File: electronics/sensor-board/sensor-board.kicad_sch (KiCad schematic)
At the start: 32 parts

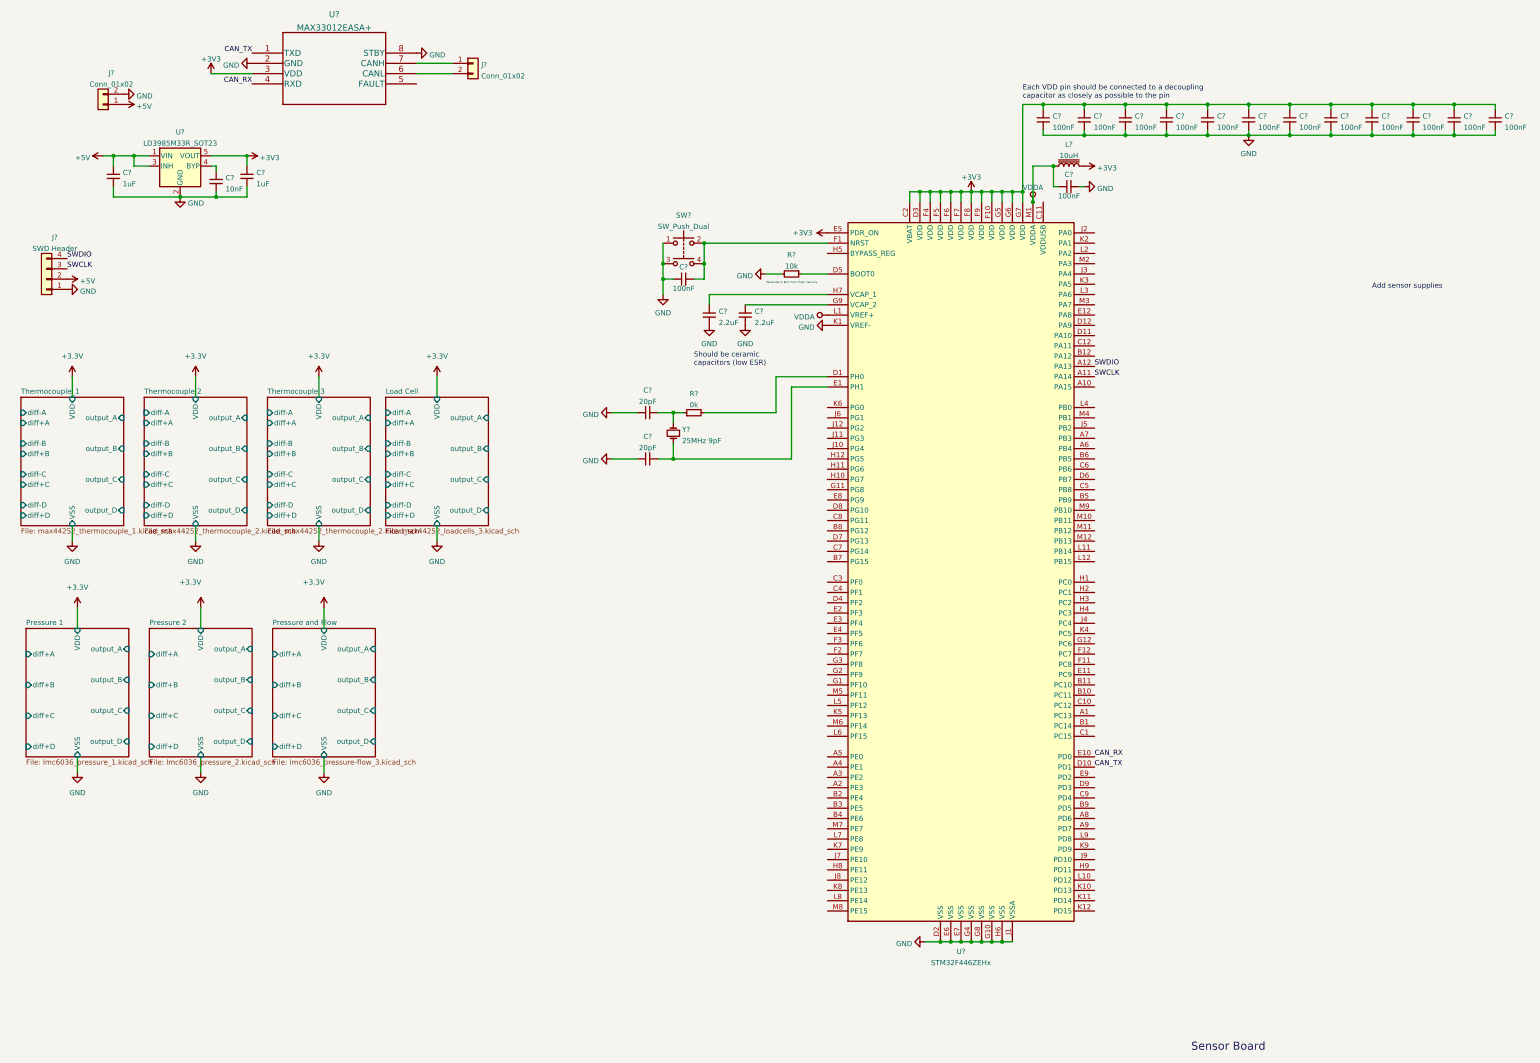
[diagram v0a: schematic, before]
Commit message: work on sensor-board
added MCP960 footprint
finished MCP960 array schematic
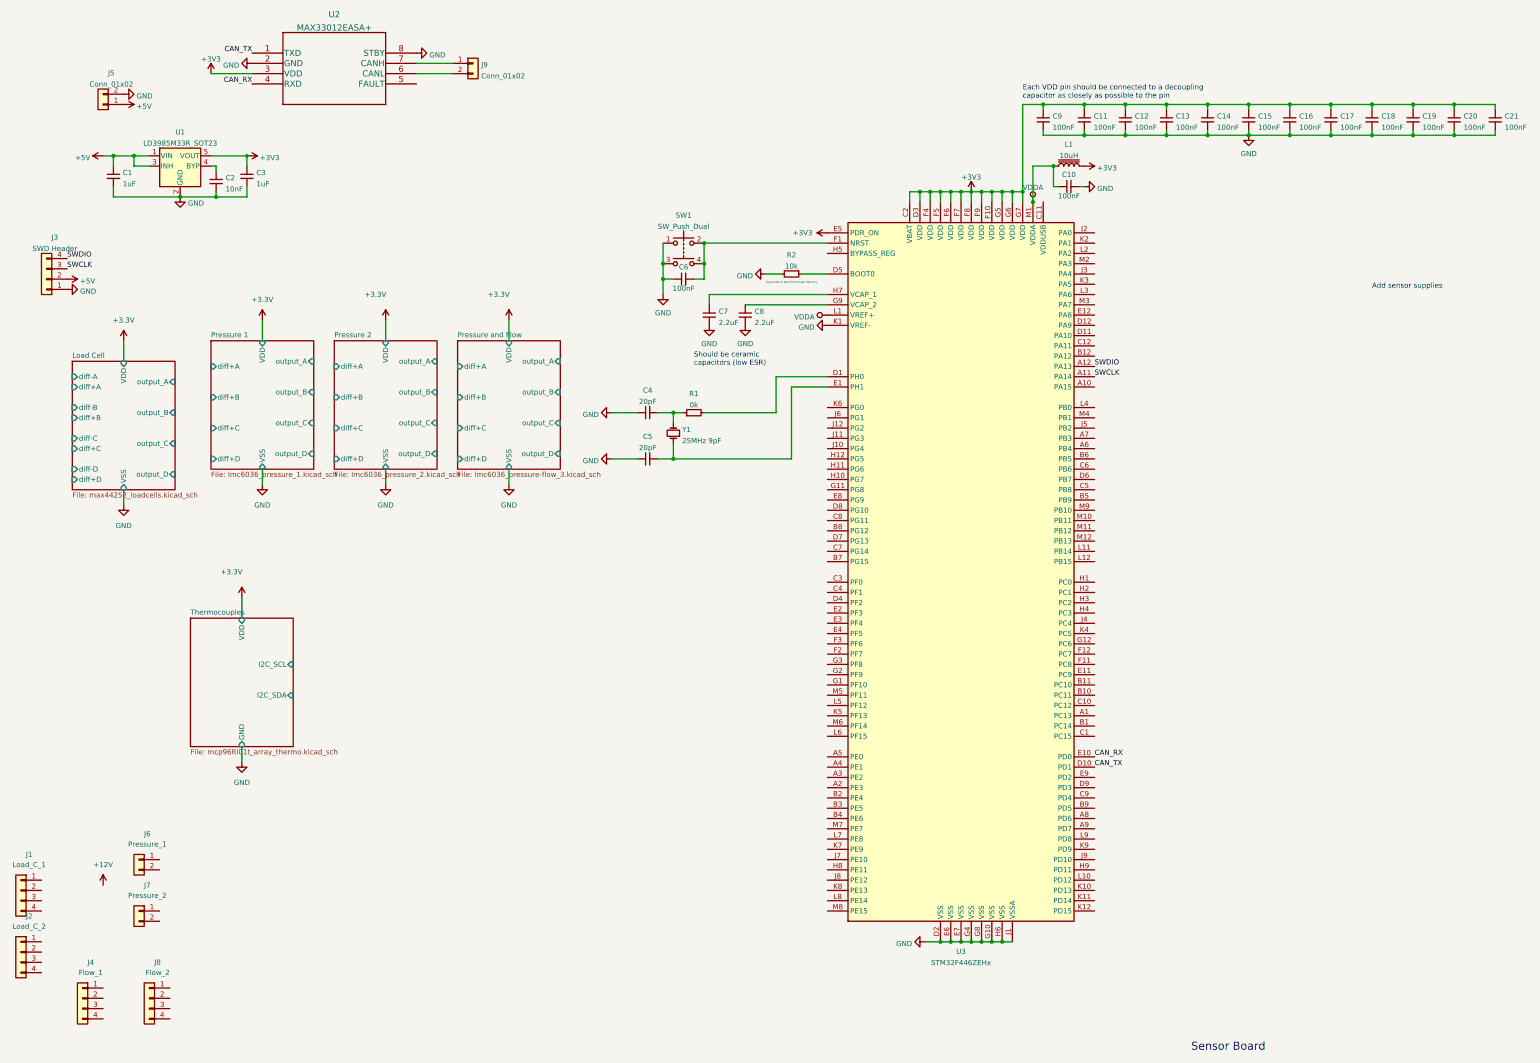
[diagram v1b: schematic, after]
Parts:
- added J1: Load_C_1, symbol Connector_Generic:Conn_01x04
- added J2: Load_C_2, symbol Connector_Generic:Conn_01x04
- added J4: Flow_1, symbol Connector_Generic:Conn_01x04
- added J6: Pressure_1, symbol Connector_Generic:Conn_01x02
- added J7: Pressure_2, symbol Connector_Generic:Conn_01x02
- added J8: Flow_2, symbol Connector_Generic:Conn_01x04
- C1, C10, C11, C12, C13, C14, C15, C16, C17, C18, C19, C2, C20, C21, C3, C4, C5, C6, C7, C8, C9: renamed from C?; footprint (none) -> Capacitor_SMD:C_0603_1608Metric
- R1, R2: renamed from R?; footprint (none) -> Resistor_SMD:R_0603_1608Metric
- U2: renamed from U?; footprint 21-0041-3-M_90-0096-8L_MXM -> MAX33012EASA+:MAX33012EASA+
- gave numbers to parts that had none: 8
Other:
- removed sheet Thermocouple 2
- removed sheet Thermocouple 3
- removed sheet Thermocouple_1
- added sheet Thermocouples (mcp96Rl01t_array_thermo.kicad_sch)
- sheet Load Cell: file max44252_loadcells_3.kicad_sch -> max44252_loadcells.kicad_sch

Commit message: work on sensor-board
thermocouple connector footprints made (selected connector)
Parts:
- added J17: Pressure_7, symbol Connector_Generic:Conn_01x02
- added J18: Pressure_8, symbol Connector_Generic:Conn_01x02
- added J19, J20: Conn_01x02, symbol Connector_Generic:Conn_01x02
- added J21: Pressure_5, symbol Connector_Generic:Conn_01x02
- added J22: Pressure_1, symbol Connector_Generic:Conn_01x02
- added J23: Pressure_2, symbol Connector_Generic:Conn_01x02
- added J24: Pressure_3, symbol Connector_Generic:Conn_01x02
- added J25: Pressure_4, symbol Connector_Generic:Conn_01x02
- J4, J8: footprint (none) -> Connector_PinHeader_2.54mm:PinHeader_1x04_P2.54mm_Horizontal
- J6: value Pressure_1 -> Pressure_5; footprint (none) -> Connector_PinHeader_2.54mm:PinHeader_1x04_P2.54mm_Horizontal
- J7: value Pressure_2 -> Pressure_6; footprint (none) -> Connector_PinHeader_2.54mm:PinHeader_1x04_P2.54mm_Horizontal
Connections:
- net +12V: now also J1.1 (Pin_1), J2.1 (Pin_1), J6.1 (Pin_1), J7.1 (Pin_1), J17.1 (Pin_1), J18.1 (Pin_1), J20.1 (Pin_1), J21.1 (Pin_1), J22.1 (Pin_1), J23.1 (Pin_1), J24.1 (Pin_1), J25.1 (Pin_1)
- net GND: now also J1.4 (Pin_4), J2.4 (Pin_4), J4.4 (Pin_4), J8.4 (Pin_4), J19.2 (Pin_2), J20.2 (Pin_2)
- net Load Cell/diff+A: now also J1.3 (Pin_3)
- net Load Cell/diff+B: now also J2.3 (Pin_3)
- net Load Cell/diff-A: now also J1.2 (Pin_2)
- net Load Cell/diff-B: now also J2.2 (Pin_2)
- net Pressure 1/diff+A: now also J22.2 (Pin_2)
- net Pressure 1/diff+B: now also J23.2 (Pin_2)
- net Pressure 1/diff+C: now also J24.2 (Pin_2)
- net Pressure 1/diff+D: now also J25.2 (Pin_2)
- net Pressure 2/diff+A: now also J6.2 (Pin_2)
- net Pressure 2/diff+B: now also J7.2 (Pin_2)
- net Pressure 2/diff+C: now also J17.2 (Pin_2)
- net Pressure 2/diff+D: now also J18.2 (Pin_2)
- net Pressure and Flow/diff+A: now also J21.2 (Pin_2)
- net Pressure and Flow/diff+B: now also J4.3 (Pin_3)
- net Pressure and Flow/diff+C: now also J8.3 (Pin_3)
- net +24V: now reaches J4.1 (Pin_1)
- net +24V: now also J8.1 (Pin_1), J19.1 (Pin_1)
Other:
- moved on the sheet: C10, C11, C12, C13, C14, C15, C16, C17, C18, C19, C20, C21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

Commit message: work on sensor-board
finishing sub-circuits
switching mcu to stm32f105
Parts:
- removed U3: STM32F446ZEHx, Package_BGA:UFBGA-144_7x7mm_Layout12x12_P0.5mm, symbol MCU_ST_STM32F4:STM32F446ZEHx
- added U? (x3): STM32F105VBH6, LFBGA100, symbol STM32F105VBH6:STM32F105VBH6
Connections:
- net +3V3: now also U?.B2 (VBAT), U?.D2 (VDD_5), U?.F4 (VDD_4), U?.F5 (VDD_3), U?.F6 (VDD_2), U?.F7 (VDD_1)
- net GND: now also U?.C2 (VSS_5), U?.E4 (VSS_4), U?.E5 (VSS_3), U?.E6 (VSS_2), U?.E7 (VSS_1), U?.G1 (VSSA), U?.H1 (VREF-)
- net VDDA: now also U?.J1 (VREF+), U?.K1 (VDDA)
- net at C5.2, Y1.1: now also U?.C1 (OSC_IN)
- net at C6.2, SW1.2, SW1.4: now also U?.E1 (NRST)
- net at R1.2: now also U?.D1 (OSC_OUT)
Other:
- note removed: "Add sensor supplies"
- moved on the sheet: C10, C11, C12, C13, C14, C15, C16, C17, C18, C19, C20, C21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

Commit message: Finalized sensor-board schematic
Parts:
- removed C13, C14, C15, C16, C17, C18, C19, C20, C21: 100nF, Capacitor_SMD:C_0603_1608Metric, symbol Device:C_Small
- removed U? (x3): STM32F105VBH6, LFBGA100, symbol STM32F105VBH6:STM32F105VBH6
- added J19: Spare_1, Connector_PinHeader_2.54mm:PinHeader_1x02_P2.54mm_Horizontal, symbol Connector_Generic:Conn_01x02
- added J20: Spare_2, Connector_PinHeader_2.54mm:PinHeader_1x02_P2.54mm_Horizontal, symbol Connector_Generic:Conn_01x02
- added J21: Spare_3, Connector_PinHeader_2.54mm:PinHeader_1x02_P2.54mm_Horizontal, symbol Connector_Generic:Conn_01x02
- added J22: Spare_4, Connector_PinHeader_2.54mm:PinHeader_1x02_P2.54mm_Horizontal, symbol Connector_Generic:Conn_01x02
- added U3: STM32L051R6Tx, Package_QFP:LQFP-64_10x10mm_P0.5mm, symbol MCU_ST_STM32L0:STM32L051R6Tx
- C7, C8: value 2.2uF -> 100nF
- J10: renamed from J5; value Conn_01x02 -> Suppply_5V; footprint (none) -> Connector_PinHeader_2.54mm:PinHeader_1x02_P2.54mm_Horizontal
- J11: renamed from J22; footprint (none) -> Connector_PinHeader_2.54mm:PinHeader_1x02_P2.54mm_Horizontal
- J12: renamed from J23; footprint (none) -> Connector_PinHeader_2.54mm:PinHeader_1x02_P2.54mm_Horizontal
- J13: renamed from J24; footprint (none) -> Connector_PinHeader_2.54mm:PinHeader_1x02_P2.54mm_Horizontal
- J14: renamed from J25; footprint (none) -> Connector_PinHeader_2.54mm:PinHeader_1x02_P2.54mm_Horizontal
- J15: renamed from J21; footprint (none) -> Connector_PinHeader_2.54mm:PinHeader_1x02_P2.54mm_Horizontal
- J18: renamed from J9; value Conn_01x02 -> CAN_Bus
- J2: renamed from J19; value Conn_01x02 -> Supply_24V; footprint (none) -> Connector_PinHeader_2.54mm:PinHeader_1x02_P2.54mm_Horizontal
- J3: renamed from J20; value Conn_01x02 -> Supply_12V; footprint (none) -> Connector_PinHeader_2.54mm:PinHeader_1x02_P2.54mm_Horizontal
- J4: renamed from J1; footprint (none) -> Connector_PinHeader_2.54mm:PinHeader_1x04_P2.54mm_Horizontal
- J5: renamed from J2; footprint (none) -> Connector_PinHeader_2.54mm:PinHeader_1x04_P2.54mm_Horizontal
- J8: renamed from J17; footprint (none) -> Connector_PinHeader_2.54mm:PinHeader_1x02_P2.54mm_Horizontal
- J9: renamed from J18; footprint (none) -> Connector_PinHeader_2.54mm:PinHeader_1x02_P2.54mm_Horizontal
- L1: footprint (none) -> Inductor_SMD:L_0603_1608Metric
- SW1: footprint (none) -> Custom_button_CS1102:Button CS1102
- renumbered J3 to J1, J4 to J16, J8 to J17
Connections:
- net +12V: now also J19.1 (Pin_1), J20.1 (Pin_1), J21.1 (Pin_1), J22.1 (Pin_1)
- net +3V3: now also C7.1, C8.1, U3.1 (VLCD), U3.19 (VDD), U3.32 (VDD), U3.48 (VDDIO2), U3.64 (VDD)
- net GND: now also U3.12 (VSSA), U3.18 (VSS), U3.31 (VSS), U3.47 (VSS), U3.63 (VSS)
- net SWCLK: now also U3.49 (PA14)
- net SWDIO: now also U3.46 (PA13)
- net VDDA: now also U3.13 (VDDA)
- net at C5.2, Y1.1: now also U3.6 (PH1)
- net at C6.2, SW1.2, SW1.4: now also U3.7 (NRST)
- net at R1.2: now also U3.5 (PH0)
- net at R2.1: now also U3.60 (BOOT0)
- new net ADC12_IN0: U3.14 (PA0)
- new net ADC12_IN1: U3.15 (PA1)
- new net ADC12_IN10: U3.8 (PC0)
- new net ADC12_IN11: U3.9 (PC1)
- new net ADC12_IN12: U3.10 (PC2)
- new net ADC12_IN13: U3.11 (PC3)
- new net ADC12_IN14: U3.24 (PC4)
- new net ADC12_IN15: U3.25 (PC5)
- new net ADC12_IN2: U3.16 (PA2)
- new net ADC12_IN3: U3.17 (PA3)
- new net ADC12_IN4: U3.20 (PA4)
- new net ADC12_IN5: U3.21 (PA5)
- new net ADC12_IN6: U3.22 (PA6)
- new net ADC12_IN7: U3.23 (PA7)
- new net ADC12_IN8: U3.26 (PB0)
- new net ADC12_IN9: U3.27 (PB1)
- new net I2C1_SCL: U3.58 (PB6)
- new net I2C1_SDA: U3.59 (PB7)
- new net I2C2_SCL: U3.29 (PB10)
- new net I2C2_SDA: U3.30 (PB11)
- new net SPARE_gen_purp_amp/diff+A: J19.2 (Pin_2)
- new net SPARE_gen_purp_amp/diff+B: J20.2 (Pin_2)
- new net SPARE_gen_purp_amp/diff+C: J21.2 (Pin_2)
- new net SPARE_gen_purp_amp/diff+D: J22.2 (Pin_2)
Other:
- added sheet SPARE_gen_purp_amp (lmc6036_pressure_SPARE.kicad_sch)
- note removed: "Should be ceramic capacitors (low ESR)"
- moved on the sheet: J1, J10, J11, J12, J13, J14, J15, J16, J17, J2, J3, J4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

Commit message: work on sensor-board
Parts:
- removed C4, C5: 20pF, Capacitor_SMD:C_0603_1608Metric, symbol Device:C_Small
- removed R1: 0k, Resistor_SMD:R_0603_1608Metric, symbol Device:R_Small
- removed R2: 10k, Resistor_SMD:R_0603_1608Metric, symbol Device:R_Small
- removed U3: STM32L051R6Tx, Package_QFP:LQFP-64_10x10mm_P0.5mm, symbol MCU_ST_STM32L0:STM32L051R6Tx
- added C27: 20pF, Capacitor_SMD:C_0603_1608Metric, symbol Device:C_Small
- added C28, C29: 100nF, Capacitor_SMD:C_0603_1608Metric, symbol Device:C_Small
- added J30: Spare_HR, Connector_PinHeader_2.54mm:PinHeader_1x04_P2.54mm_Horizontal, symbol Connector_Generic:Conn_01x04
- added R108, R2: TO CALCULATE 4.7k, Resistor_SMD:R_0603_1608Metric, symbol Device:R
- added R109, R110: 100, Resistor_SMD:R_0603_1608Metric, symbol Device:R
- added R111: 10k, Resistor_SMD:R_0603_1608Metric, symbol Device:R_Small
- added R112: 0k, Resistor_SMD:R_0603_1608Metric, symbol Device:R_Small
- added U3: STM32F105VBH6, STM32F105VBH6:STM32F105VBH6, symbol STM32F105VBH6:STM32F105VBH6
- C12: value 100nF -> 20pF
- J15: value Pressure_5 -> Pressure_9
- J18, Y1: footprint (none) -> Resistor_THT:R_Axial_DIN0204_L3.6mm_D1.6mm_P1.90mm_Vertical
- J6, J7: footprint Connector_PinHeader_2.54mm:PinHeader_1x04_P2.54mm_Horizontal -> Connector_PinHeader_2.54mm:PinHeader_1x02_P2.54mm_Horizontal
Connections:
- net +12V: now also J30.1 (Pin_1)
- net +3V3: now also C10.1, C6.1, C29.1, U3.B2 (VBAT), U3.D2 (VDD_5), U3.F4 (VDD_4), U3.F5 (VDD_3), U3.F6 (VDD_2), U3.F7 (VDD_1); no longer C12.1, C8.1
- net ADC12_IN0: now also U3.G2 (PA0-WKUP)
- net ADC12_IN1: now also U3.H2 (PA1)
- net ADC12_IN10: now also U3.F1 (PC0)
- net ADC12_IN11: now also U3.F2 (PC1)
- net ADC12_IN12: now also U3.E2 (PC2)
- net ADC12_IN13: now also U3.F3 (PC3)
- net ADC12_IN14: now also U3.G4 (PC4)
- net ADC12_IN15: now also U3.H4 (PC5)
- net ADC12_IN2: now also U3.J2 (PA2)
- net ADC12_IN3: now also U3.K2 (PA3)
- net ADC12_IN4: now also U3.G3 (PA4)
- net ADC12_IN5: now also U3.H3 (PA5)
- net ADC12_IN6: now also U3.J3 (PA6)
- net ADC12_IN7: now also U3.K3 (PA7)
- net ADC12_IN8: now also U3.J4 (PB0)
- net ADC12_IN9: now also U3.K4 (PB1)
- net CAN_RX: now also U3.C10 (PA11)
- net CAN_TX: now also U3.B10 (PA12)
- net GND: now also C12.1, C6.2, C27.1, C28.1, C29.2, J30.4 (Pin_4), R111.2, U3.C2 (VSS_5), U3.E4 (VSS_4), U3.E5 (VSS_3), U3.E6 (VSS_2), U3.E7 (VSS_1), U3.G1 (VSSA), U3.H1 (VREF-); no longer C12.2, C6.1
- net I2C1_SCL: now also R109.1, R2.2
- net I2C1_SDA: now also R108.2, R110.1
- net I2C2_SCL: now also U3.J7 (PB10)
- net I2C2_SDA: now also U3.K7 (PB11)
- net Load Cell/diff+C: now also J30.3 (Pin_3)
- net Load Cell/diff-C: now also J30.2 (Pin_2)
- net SWCLK: now also U3.A9 (PA14)
- net SWDIO: now also U3.A10 (PA13)
- net VDDA: now also C8.1, U3.J1 (VREF+), U3.K1 (VDDA); no longer C10.1
- net at Y1.1: now also C12.2, U3.C1 (OSC_IN)
- net at Y1.2: now also C27.2, R112.1
- net at SW1.2, SW1.4: now also C28.2, U3.E1 (NRST); no longer C6.2
- new net: R112.2, U3.D1 (OSC_OUT)
- new net: R110.2, U3.A5 (PB7)
- new net: R109.2, U3.B5 (PB6)
- new net: R111.1, U3.D5 (BOOT0)
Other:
- note added: "NOT USED"
- note removed: "Hardcode to boot from flash memory"
- moved on the sheet: J1, J10, J4, J5

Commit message: work on sensor-board pcb
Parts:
- removed Y1: 25MHz 9pF, Resistor_THT:R_Axial_DIN0204_L3.6mm_D1.6mm_P1.90mm_Vertical, symbol Device:Crystal_Small
- added Y1: Crystal_GND24, Crystal:Crystal_SMD_3225-4Pin_3.2x2.5mm, symbol Device:Crystal_GND24
- J18: footprint Resistor_THT:R_Axial_DIN0204_L3.6mm_D1.6mm_P1.90mm_Vertical -> Connector_PinHeader_2.54mm:PinHeader_1x02_P2.54mm_Horizontal
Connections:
- net GND: now also Y1.1, Y1.3
- net at C27.2, R112.1: now also Y1.4
- net at C12.2, U3.C1 (OSC_IN): now also Y1.2
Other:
- moved on the sheet: C27, R112

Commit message: work on sensor-board pcb
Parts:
- added J31: Spare_HR_2, Custom_Molex_SL_2.54:SL_2.54_H_4pin, symbol Connector_Generic:Conn_01x04
- added TP1, TP2, TP3, TP4, TP5, TP6, TP7: TestPoint, TestPoint:TestPoint_Pad_D2.0mm, symbol Connector:TestPoint
- J10, J11, J12, J13, J14, J15, J18, J19, J2, J20, J21, J22, J3, J6, J7, J8, J9: footprint Connector_PinHeader_2.54mm:PinHeader_1x02_P2.54mm_Horizontal -> Custom_Molex_SL_2.54:SL_2.54_H_2pin
- J16, J17, J4, J5: footprint Connector_PinHeader_2.54mm:PinHeader_1x04_P2.54mm_Horizontal -> Custom_Molex_SL_2.54:SL_2.54_H_4pin
- J30: value Spare_HR -> Spare_HR_1; footprint Connector_PinHeader_2.54mm:PinHeader_1x04_P2.54mm_Horizontal -> Custom_Molex_SL_2.54:SL_2.54_H_4pin
- R108, R2: value TO CALCULATE 4.7k -> 4.7k
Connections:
- net +12V: now also J31.1 (Pin_1); no longer J19.1 (Pin_1), J20.1 (Pin_1), J21.1 (Pin_1), J22.1 (Pin_1)
- net +3V3: now also R108.1, R2.1
- net ADC12_IN13: now also TP5.1
- net ADC12_IN14: now also TP6.1
- net ADC12_IN15: now also TP7.1
- net GND: now also J31.4 (Pin_4)
- net Load Cell/diff+D: now also J31.3 (Pin_3)
- net Load Cell/diff-D: now also J31.2 (Pin_2)
- net SPARE_gen_purp_amp/output_B: now also TP2.1
- net SPARE_gen_purp_amp/output_C: now also TP3.1
- net SPARE_gen_purp_amp/output_D: now also TP4.1
- new net SPARE_gen_purp_amp/diff-A: J19.1 (Pin_1)
- new net SPARE_gen_purp_amp/diff-B: J20.1 (Pin_1)
- new net SPARE_gen_purp_amp/diff-C: J21.1 (Pin_1)
- new net SPARE_gen_purp_amp/diff-D: J22.1 (Pin_1)
- new net SPARE_gen_purp_amp/output_A: TP1.1
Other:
- sheet SPARE_gen_purp_amp ports: added diff-A, diff-B, diff-C, diff-D; removed none
- moved on the sheet: J10, J2, J3, J30, J4, J5

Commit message: work on sensor-board
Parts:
- removed TP7: TestPoint, TestPoint:TestPoint_Pad_D2.0mm, symbol Connector:TestPoint
